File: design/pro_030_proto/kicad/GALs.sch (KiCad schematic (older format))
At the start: 15 parts, among them IC2 ATF22V10C, IC3 ATF22V10C, IC4 ATF22V10C, IC5 ATF22V10C, IC6 ATF22V10C, IC7 ATF22V10C

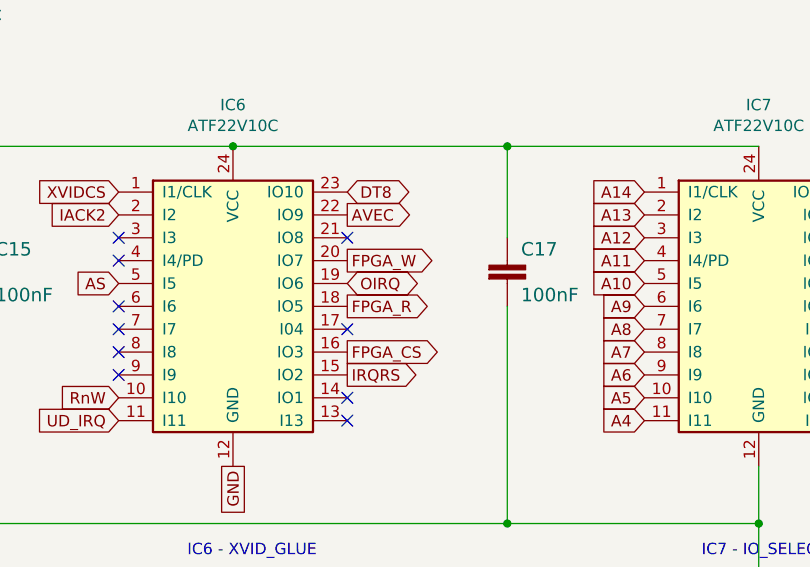
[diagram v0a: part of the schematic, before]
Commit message: First cut placement
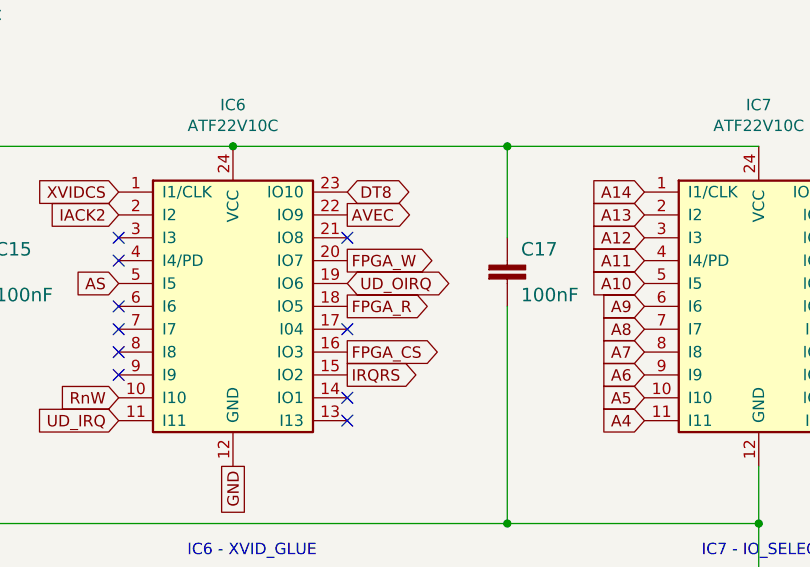
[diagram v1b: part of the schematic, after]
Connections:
- net OIRQ renamed UD_OIRQ
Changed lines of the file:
@@
 FPGA_W
 Text GLabel 2900 4800 2    50   3State ~ 0
-OIRQ
+UD_OIRQ
 NoConn ~ 2900 5000
 Text GLabel 2900 4900 2    50   Output ~ 0

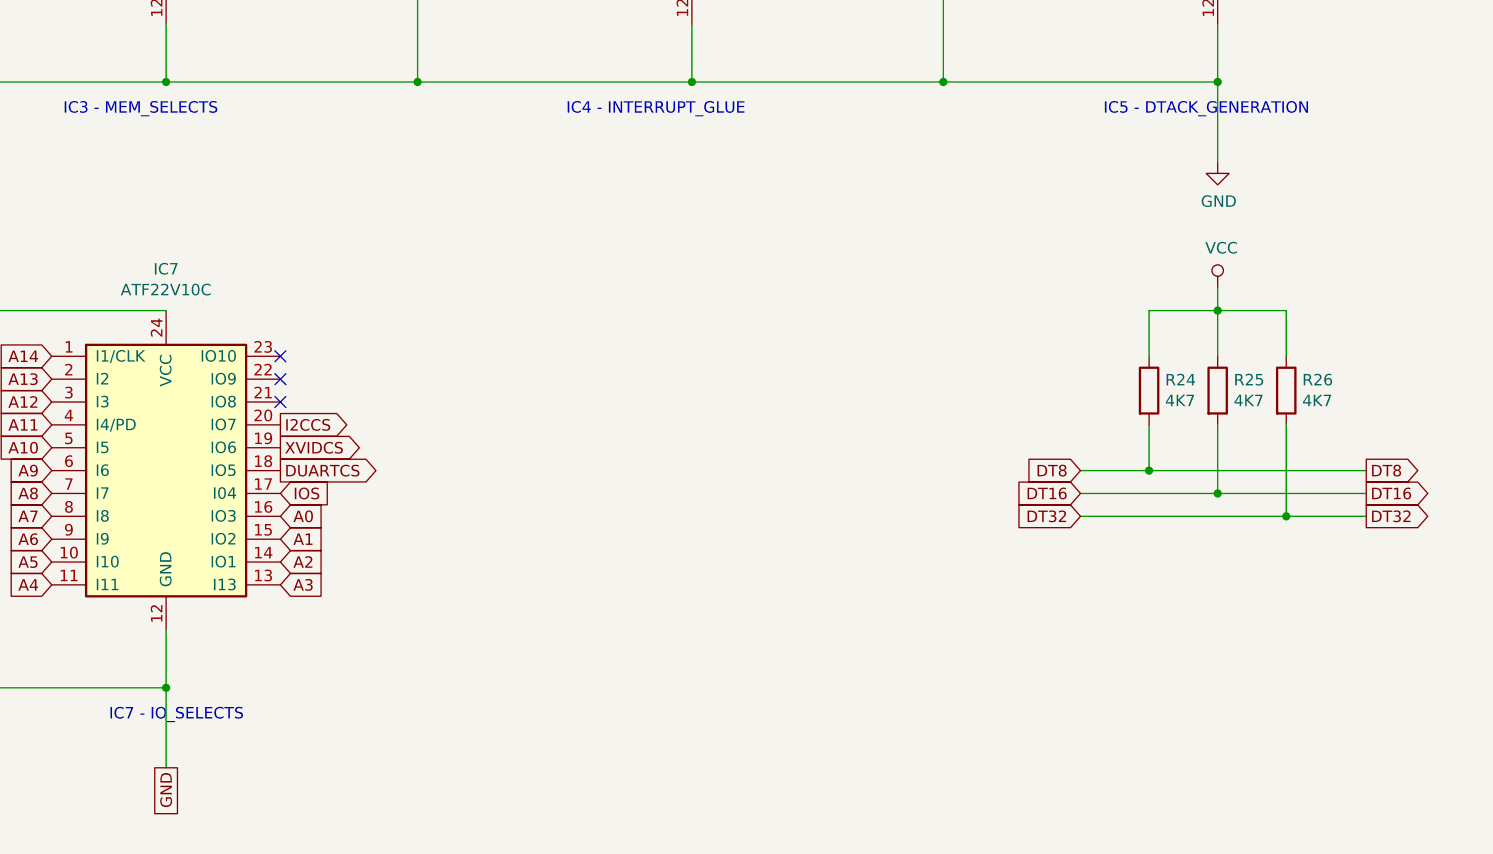
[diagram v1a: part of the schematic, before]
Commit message: Replace 7493s and 7404 with IC10 GAL
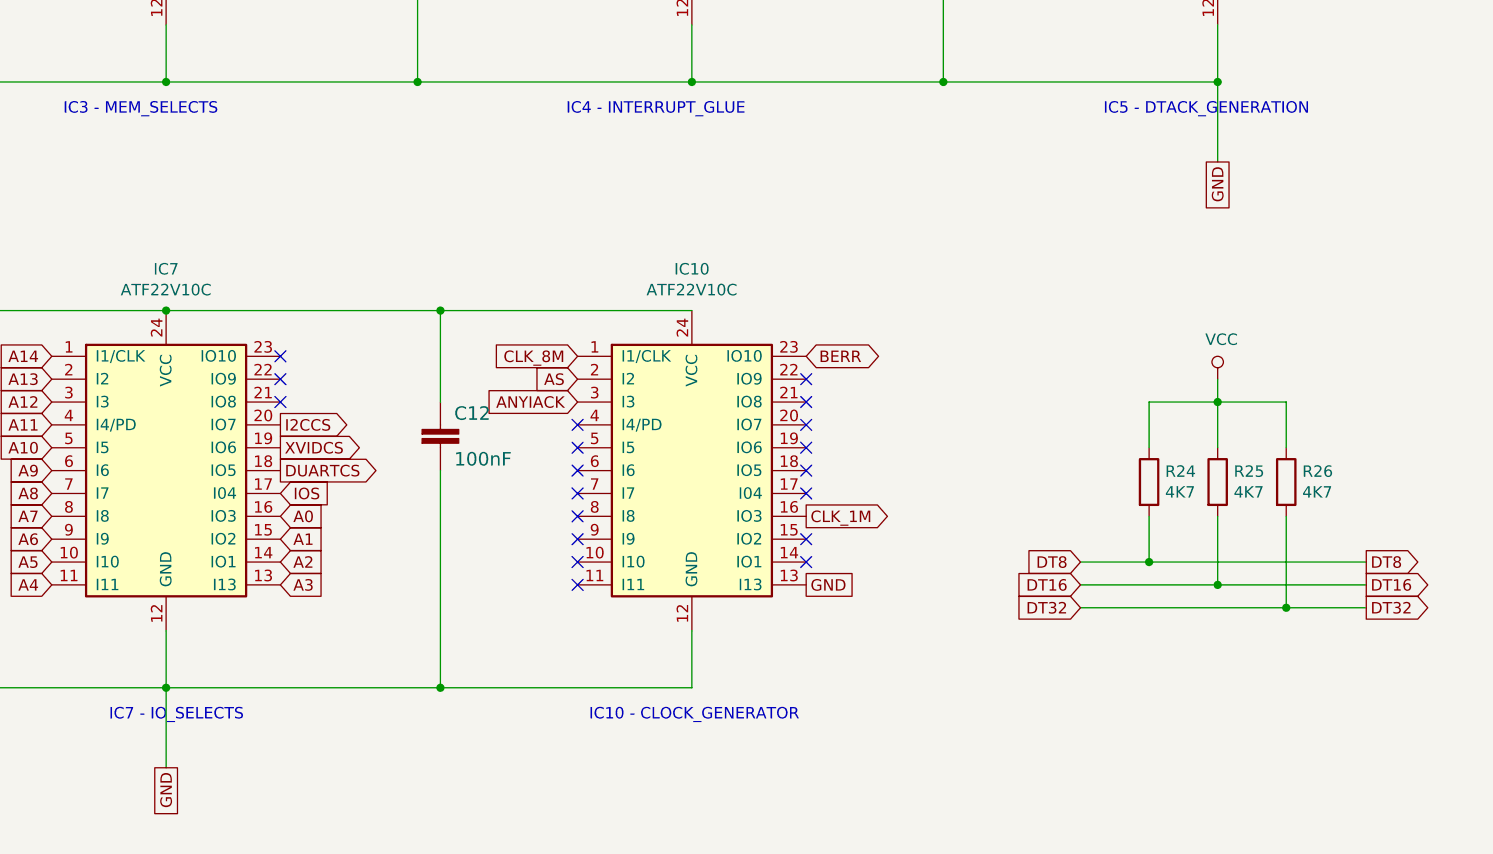
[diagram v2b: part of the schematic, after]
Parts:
- added C12: 100nF, Capacitor_THT:C_Rect_L4.0mm_W2.5mm_P2.50mm, symbol rosco_m68k-eagle-import:C2,5-3
- added IC10: ATF22V10C, Package_DIP:DIP-24_W7.62mm_Socket_LongPads, symbol rosco_m68k:GAL22V10
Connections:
- net ANYIACK: now also IC10.3 (I3)
- net AS: now also IC10.2 (I2)
- net GND: now also C12.2, IC10.12 (GND), IC10.13 (I13)
- net VCC: now also C12.1, IC10.24 (VCC)
- new net BERR: IC10.23 (IO10)
- new net CLK_1M: IC10.16 (IO3)
- new net CLK_8M: IC10.1 (I1/CLK)
- no-connect marks 28 -> 44
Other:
- note added: "IC10 - CLOCK_GENERATOR"
- moved on the sheet: R24, R25, R26
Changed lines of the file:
@@
 NoConn ~ 8800 2650
 NoConn ~ 8800 2750
-Text GLabel 8700 4900 0    50   Input ~ 0
+Text GLabel 8700 5300 0    50   Input ~ 0
 DT8
-Text GLabel 8700 5000 0    50   Input ~ 0
+Text GLabel 8700 5400 0    50   Input ~ 0
 DT16
-Text GLabel 8700 5100 0    50   Input ~ 0
+Text GLabel 8700 5500 0    50   Input ~ 0
 DT32
-Text GLabel 9950 4900 2    50   Output ~ 0
+Text GLabel 9950 5300 2    50   Output ~ 0
 DT8
-Text GLabel 9950 5000 2    50   Output ~ 0
+Text GLabel 9950 5400 2    50   Output ~ 0
 DT16
-Text GLabel 9950 5100 2    50   Output ~ 0
+Text GLabel 9950 5500 2    50   Output ~ 0
 DT32
 $Comp
 L Device:R R24
 U 1 1 60FCD0F0
-P 9000 4550
-F 0 "R24" H 9070 4596 50  0000 L CNN
-F 1 "4K7" H 9070 4505 50  0000 L CNN
-F 2 "rosco_m68k:R-0207_10" V 8930 4550 50  0001 C CNN
-F 3 "~" H 9000 4550 50  0001 C CNN
-	1    9000 4550
+P 9000 4950
+F 0 "R24" H 9070 4996 50  0000 L CNN
+F 1 "4K7" H 9070 4905 50  0000 L CNN
+F 2 "rosco_m68k:R-0207_10" V 8930 4950 50  0001 C CNN
+F 3 "~" H 9000 4950 50  0001 C CNN
+	1    9000 4950
 	1    0    0    -1
 $EndComp
@@
 L Device:R R25
 U 1 1 60FCDD0E
-P 9300 4550
-F 0 "R25" H 9370 4596 50  0000 L CNN
-F 1 "4K7" H 9370 4505 50  0000 L CNN
-F 2 "rosco_m68k:R-0207_10" V 9230 4550 50  0001 C CNN
-F 3 "~" H 9300 4550 50  0001 C CNN
-	1    9300 4550
+P 9300 4950
+F 0 "R25" H 9370 4996 50  0000 L CNN
+F 1 "4K7" H 9370 4905 50  0000 L CNN
+F 2 "rosco_m68k:R-0207_10" V 9230 4950 50  0001 C CNN
+F 3 "~" H 9300 4950 50  0001 C CNN
+	1    9300 4950
 	1    0    0    -1
 $EndComp
@@
 L Device:R R26
 U 1 1 60FCE353
-P 9600 4550
-F 0 "R26" H 9670 4596 50  0000 L CNN
-F 1 "4K7" H 9670 4505 50  0000 L CNN
-F 2 "rosco_m68k:R-0207_10" V 9530 4550 50  0001 C CNN
-F 3 "~" H 9600 4550 50  0001 C CNN
-	1    9600 4550
+P 9600 4950
+F 0 "R26" H 9670 4996 50  0000 L CNN
+F 1 "4K7" H 9670 4905 50  0000 L CNN
+F 2 "rosco_m68k:R-0207_10" V 9530 4950 50  0001 C CNN
+F 3 "~" H 9600 4950 50  0001 C CNN
+	1    9600 4950
 	1    0    0    -1
 $EndComp
@@
 L power:VCC #PWR033
 U 1 1 60FCF006
-P 9300 4100
-F 0 "#PWR033" H 9300 3950 50  0001 C CNN
-F 1 "VCC" H 9317 4273 50  0000 C CNN
-F 2 "" H 9300 4100 50  0001 C CNN
-F 3 "" H 9300 4100 50  0001 C CNN
-	1    9300 4100
-	1    0    0    -1
-$EndComp
-Wire Wire Line
-	9000 4400 9000 4200
-Wire Wire Line
-	9000 4200 9300 4200
-Wire Wire Line
-	9300 4200 9300 4100
-Wire Wire Line
-	9300 4200 9600 4200
-Wire Wire Line
-	9600 4200 9600 4400
-Connection ~ 9300 4200
-Wire Wire Line
-	8700 4900 9000 4900
-Wire Wire Line
-	8700 5000 9300 5000
-Wire Wire Line
-	8700 5100 9600 5100
-Wire Wire Line
-	9000 4700 9000 4900
-Connection ~ 9000 4900
-Wire Wire Line
-	9000 4900 9950 4900
-Wire Wire Line
-	9300 4700 9300 5000
-Connection ~ 9300 5000
-Wire Wire Line
-	9300 5000 9950 5000
-Wire Wire Line
-	9600 4700 9600 5100
-Connection ~ 9600 5100
-Wire Wire Line
-	9600 5100 9950 5100
+P 9300 4500
+F 0 "#PWR033" H 9300 4350 50  0001 C CNN
+F 1 "VCC" H 9317 4673 50  0000 C CNN
+F 2 "" H 9300 4500 50  0001 C CNN
+F 3 "" H 9300 4500 50  0001 C CNN
+	1    9300 4500
+	1    0    0    -1
+$EndComp
+Wire Wire Line
+	9000 4800 9000 4600
+Wire Wire Line
+	9000 4600 9300 4600
+Wire Wire Line
+	9300 4600 9300 4500
+Wire Wire Line
+	9300 4600 9600 4600
+Wire Wire Line
+	9600 4600 9600 4800
+Connection ~ 9300 4600
+Wire Wire Line
+	8700 5300 9000 5300
+Wire Wire Line
+	8700 5400 9300 5400
+Wire Wire Line
+	8700 5500 9600 5500
+Wire Wire Line
+	9000 5100 9000 5300
+Connection ~ 9000 5300
+Wire Wire Line
+	9000 5300 9950 5300
+Wire Wire Line
+	9300 5100 9300 5400
+Connection ~ 9300 5400
+Wire Wire Line
+	9300 5400 9950 5400
+Wire Wire Line
+	9600 5100 9600 5500
+Connection ~ 9600 5500
+Wire Wire Line
+	9600 5500 9950 5500
 Text GLabel 8800 1750 0    50   Input ~ 0
 RAMS
@@
 BOOT
 Wire Wire Line
-	9300 4200 9300 4400
+	9300 4600 9300 4800
 Wire Wire Line
 	2400 4200 3600 4200
@@
 	3600 4600 3600 4200
 Connection ~ 3600 4200
-Wire Wire Line
-	3600 4200 4700 4200
 Wire Wire Line
 	1300 3800 1300 4200
@@
 Wire Wire Line
 	7000 3200 8100 3200
-$Comp
-L power:GND #PWR0102
-U 1 1 616CEF14
-P 9300 3550
-F 0 "#PWR0102" H 9300 3300 50  0001 C CNN
-F 1 "GND" H 9305 3377 50  0000 C CNN
-F 2 "" H 9300 3550 50  0001 C CNN
-F 3 "" H 9300 3550 50  0001 C CNN
-	1    9300 3550
-	1    0    0    -1
-$EndComp
 Wire Wire Line
 	4700 5850 4700 6200
@@
 Text GLabel 5200 4700 2    50   Output ~ 0
 I2CCS
+$Comp
+L rosco_m68k:GAL22V10 IC?
+U 1 1 616244B8
+P 7000 4900
+AR Path="/61161E57/616244B8" Ref="IC?"  Part="1"
+AR Path="/6103896C/616244B8" Ref="IC10"  Part="1"
+F 0 "IC10" H 7000 5781 50  0000 C CNN
+F 1 "ATF22V10C" H 7000 5690 50  0000 C CNN
+F 2 "Package_DIP:DIP-24_W7.62mm_Socket_LongPads" H 7000 4900 50  0001 C CNN
+F 3 "https://www.mouser.com/datasheet/2/268/doc0735-1369018.pdf" H 7000 4900 50  0001 C CNN
+	1    7000 4900
+	1    0    0    -1
+$EndComp
+Wire Wire Line
+	7000 5600 7000 5850
+Text GLabel 6500 4400 0    50   Input ~ 0
+CLK_8M
+Text GLabel 6500 4500 0    50   Input ~ 0
+AS
+Text GLabel 6500 4600 0    50   Input ~ 0
+ANYIACK
+NoConn ~ 7500 4600
+NoConn ~ 7500 4500
+Text Notes 6550 6000 0    50   ~ 0
+IC10 - CLOCK_GENERATOR
+$Comp
+L rosco_m68k-eagle-import:C2,5-3 C?
+U 1 1 616269B3
+P 5900 4700
+AR Path="/616269B3" Ref="C?"  Part="1"
+AR Path="/5E53B810/616269B3" Ref="C?"  Part="1"
+AR Path="/5E53B952/616269B3" Ref="C?"  Part="1"
+AR Path="/6103896C/616269B3" Ref="C12"  Part="1"
+F 0 "C12" H 5960 4715 59  0000 L BNN
+F 1 "100nF" H 5960 4515 59  0000 L BNN
+F 2 "Capacitor_THT:C_Rect_L4.0mm_W2.5mm_P2.50mm" H 5900 4700 50  0001 C CNN
+F 3 "" H 5900 4700 50  0001 C CNN
+	1    5900 4700
+	1    0    0    -1
+$EndComp
+Wire Wire Line
+	5900 4900 5900 5850
+Wire Wire Line
+	4700 5850 5900 5850
+Wire Wire Line
+	7000 5850 5900 5850
+Connection ~ 5900 5850
+Wire Wire Line
+	5900 4200 5900 4600
+Wire Wire Line
+	3600 4200 4700 4200
+Connection ~ 4700 4200
+Wire Wire Line
+	4700 4200 5900 4200
+Text GLabel 9300 3550 3    50   UnSpc ~ 0
+GND
+Wire Wire Line
+	5900 4200 7000 4200
+Connection ~ 5900 4200
+NoConn ~ 6500 4700
+NoConn ~ 6500 4800
+NoConn ~ 6500 4900
+NoConn ~ 6500 5000
+NoConn ~ 6500 5100
+NoConn ~ 6500 5200
+NoConn ~ 6500 5300
+NoConn ~ 6500 5400
+Text GLabel 7500 5100 2    50   Output ~ 0
+CLK_1M
+Text GLabel 7500 5400 2    50   UnSpc ~ 0
+GND
+Text GLabel 7500 4400 2    50   3State ~ 0
+BERR
+NoConn ~ 7500 5300
+NoConn ~ 7500 5200
+NoConn ~ 7500 5000
+NoConn ~ 7500 4900
+NoConn ~ 7500 4800
+NoConn ~ 7500 4700
 $EndSCHEMATC
